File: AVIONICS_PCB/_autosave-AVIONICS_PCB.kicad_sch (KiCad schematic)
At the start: 5 parts, among them U1 ESP32-S3-DevKitC

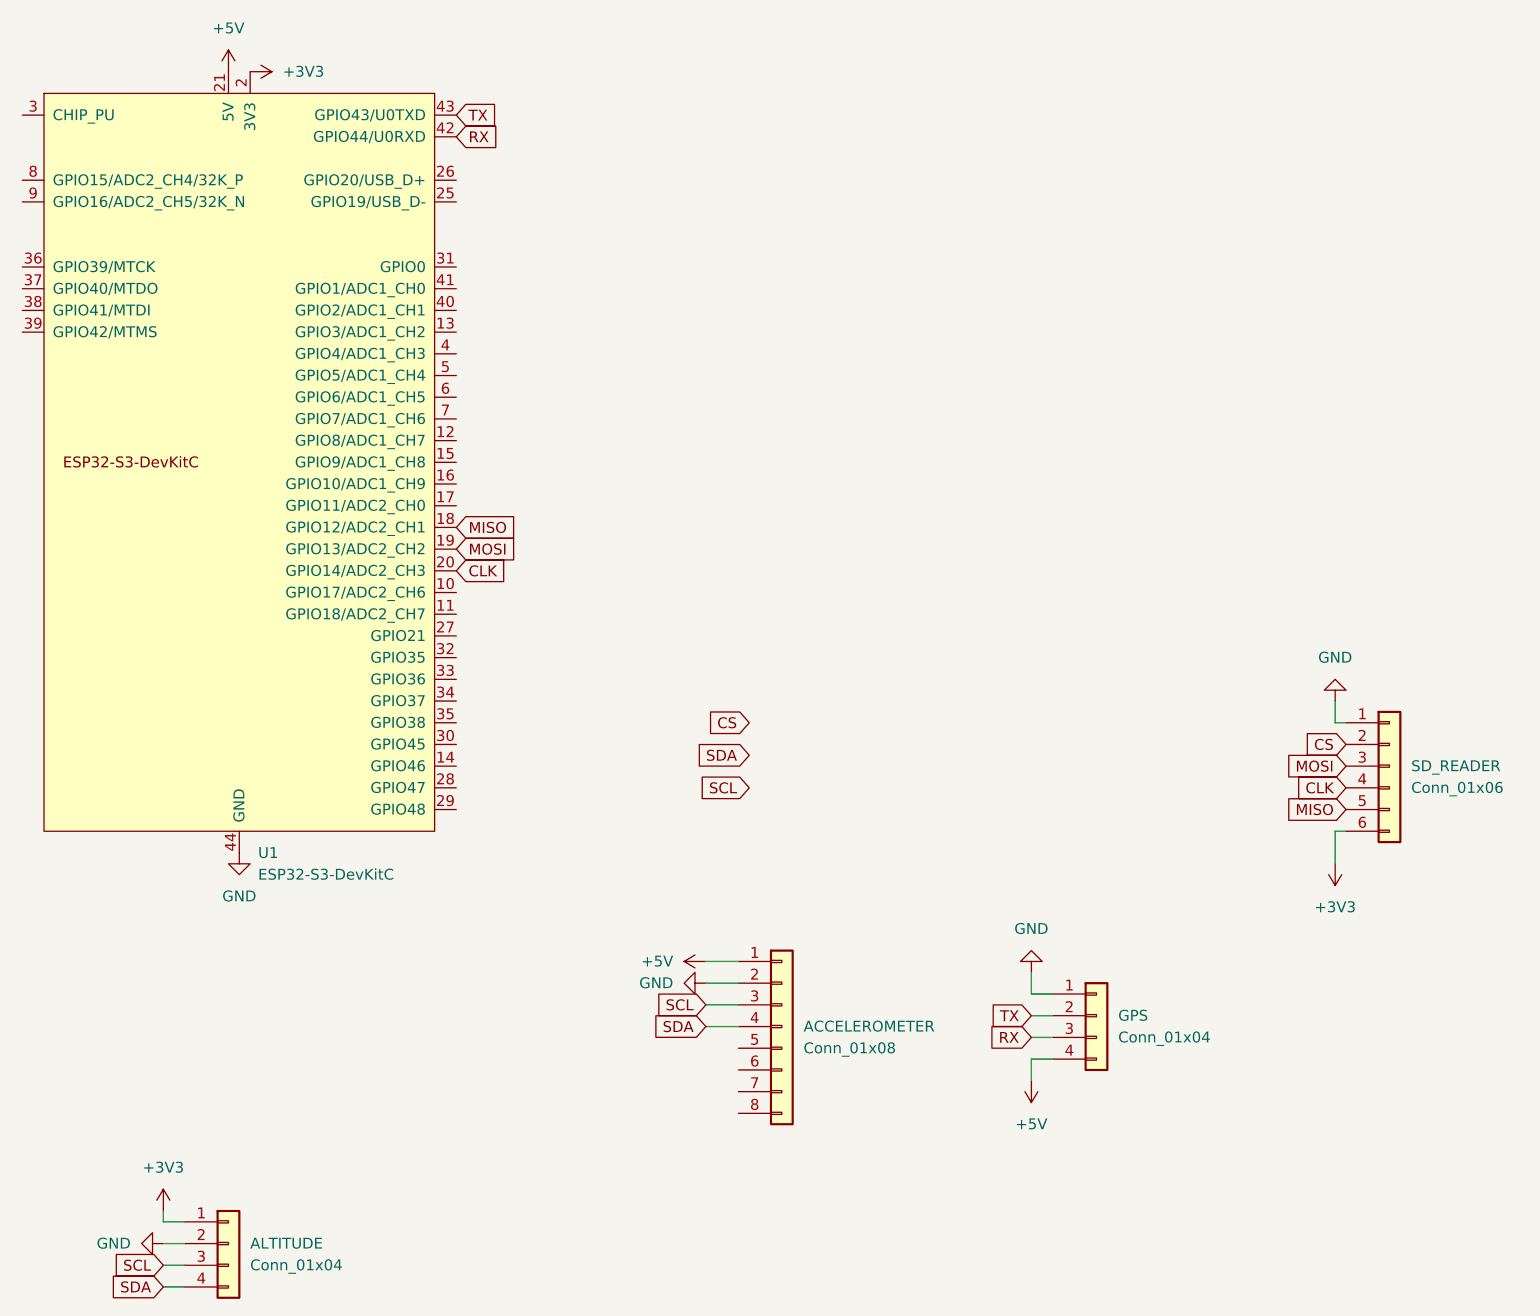
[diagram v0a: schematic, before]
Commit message: Started footprint layout
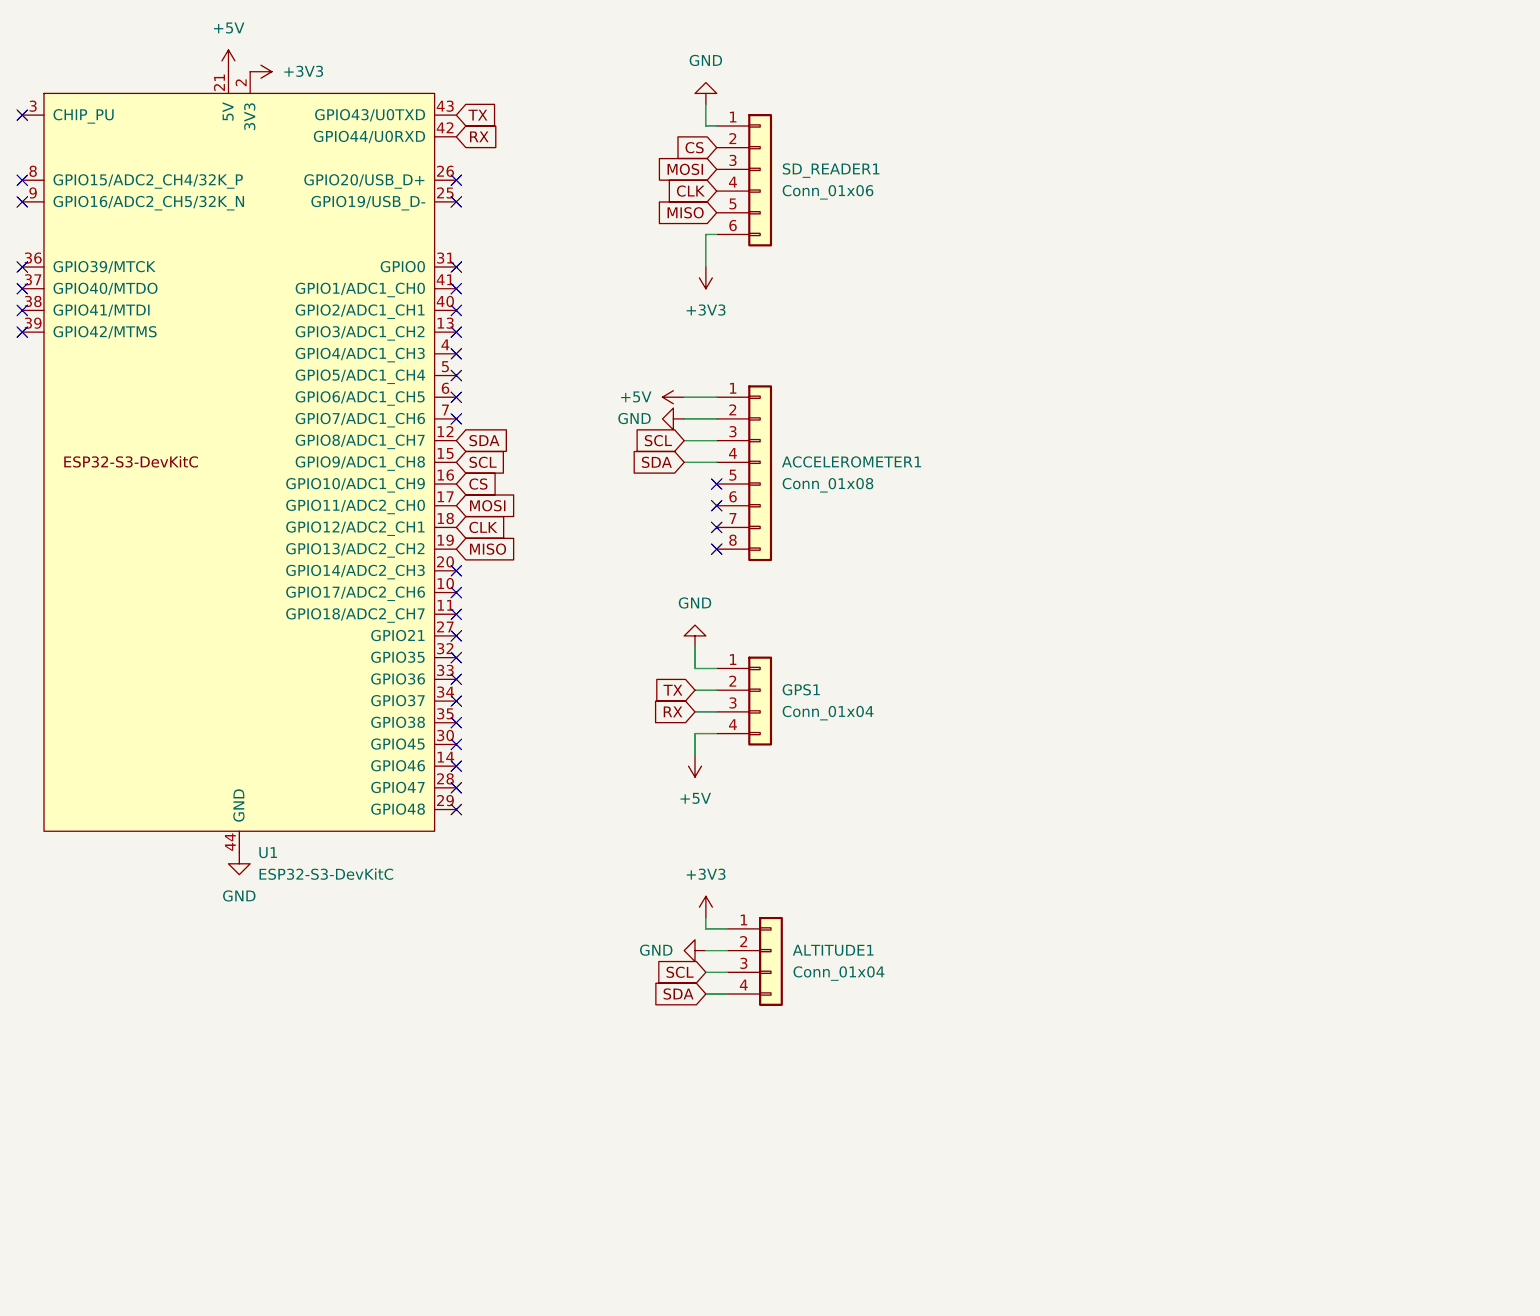
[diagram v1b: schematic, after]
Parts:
- renumbered ACCELEROMETER to ACCELEROMETER1, ALTITUDE to ALTITUDE1, GPS to GPS1, SD_READER to SD_READER1
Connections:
- net CLK: now also U1.18 (GPIO12/ADC2_CH1); no longer U1.20 (GPIO14/ADC2_CH3)
- net CS: now also U1.16 (GPIO10/ADC1_CH9)
- net MISO: now also U1.19 (GPIO13/ADC2_CH2); no longer U1.18 (GPIO12/ADC2_CH1)
- net MOSI: now also U1.17 (GPIO11/ADC2_CH0); no longer U1.19 (GPIO13/ADC2_CH2)
- net SCL: now also U1.15 (GPIO9/ADC1_CH8)
- net SDA: now also U1.12 (GPIO8/ADC1_CH7)
- no-connect marks 0 -> 33
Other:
- moved on the sheet: ACCELEROMETER1, ALTITUDE1, GPS1, SD_READER1
